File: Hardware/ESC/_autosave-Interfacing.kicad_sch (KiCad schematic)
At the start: 41 parts, among them U2 DRV8300UDRGER, U3 INA4180A2IPWR, U7 LM339

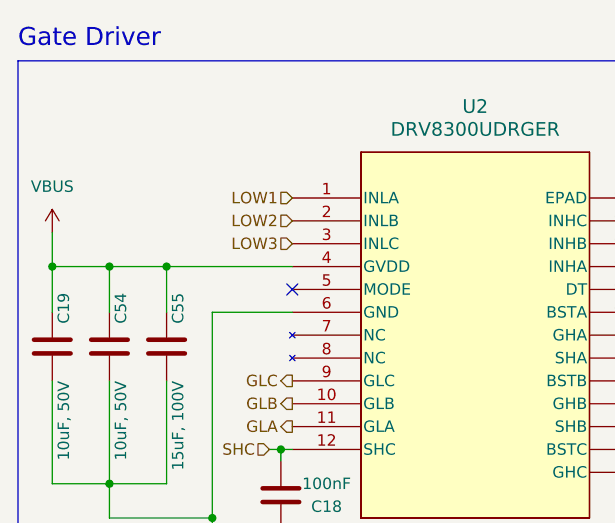
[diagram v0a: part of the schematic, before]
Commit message: Breaking + BEMF ZCD Detector
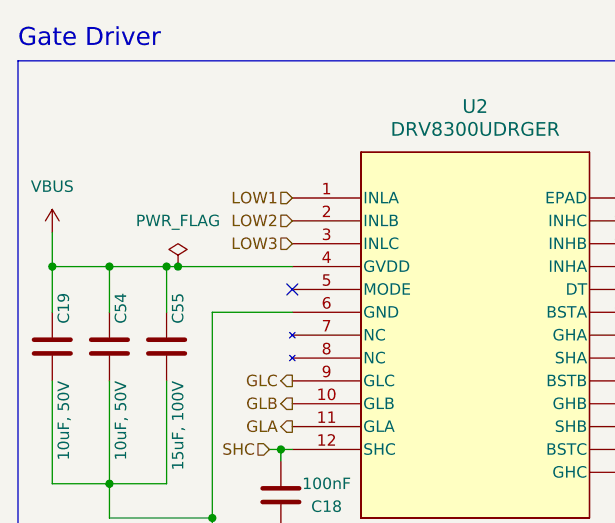
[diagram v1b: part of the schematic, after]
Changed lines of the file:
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@@
   (junction (at 132.08 139.7) (diameter 0) (color 0 0 0 0)
+  )
+  (junction (at 39.37 48.26) (diameter 0) (color 0 0 0 0)
   )
   (junction (at 31.75 72.39) (diameter 0) (color 0 0 0 0)
@@
     (stroke (width 0) (type default))
   )
-  (wire (pts (xy 38.1 48.26) (xy 52.07 48.26))
+  (wire (pts (xy 38.1 48.26) (xy 39.37 48.26))
     (stroke (width 0) (type default))
   )
@@
   )
   (wire (pts (xy 251.46 38.1) (xy 251.46 43.18))
+    (stroke (width 0) (type default))
+  )
+  (wire (pts (xy 39.37 48.26) (xy 52.07 48.26))
     (stroke (width 0) (type default))
   )
@@
     )
   )
+  (symbol (lib_id "power:PWR_FLAG") (at 39.37 48.26 0) (unit 1)
+    (in_bom yes) (on_board yes) (dnp no) (fields_autoplaced)
+    (property "Reference" "#FLG03" (at 39.37 46.355 0)
+      (effects (font (size 1.27 1.27)) hide)
+    )
+    (property "Value" "PWR_FLAG" (at 39.37 43.18 0)
+      (effects (font (size 1.27 1.27)))
+    )
+    (property "Footprint" "" (at 39.37 48.26 0)
+      (effects (font (size 1.27 1.27)) hide)
+    )
+    (property "Datasheet" "~" (at 39.37 48.26 0)
+      (effects (font (size 1.27 1.27)) hide)
+    )
+    (pin "1")
+    (instances
+      (project "BLDC_ESC"
+        (path "/bd67e774-828f-47d6-928d-7f9ad42d6cab/833552ae-4955-4bf3-a78a-8c8ee4e0e417"
+          (reference "#FLG03") (unit 1)
+        )
+      )
+    )
+  )
   (symbol (lib_id "Device:C") (at 199.39 49.53 0) (unit 1)
     (in_bom yes) (on_board yes) (dnp no) (fields_autoplaced)
@@
     )
   )
+  (symbol (lib_id "Driver_Motor:DRV8300UDRGER") (at 52.07 40.64 0) (unit 1)
+    (in_bom yes) (on_board yes) (dnp no) (fields_autoplaced)
+    (property "Reference" "U2" (at 72.39 30.48 0)
+      (effects (font (size 1.524 1.524)))
+    )
+    (property "Value" "DRV8300UDRGER" (at 72.39 33.02 0)
+      (effects (font (size 1.524 1.524)))
+    )
+    (property "Footprint" "WQFN_0DRGER_TEX" (at 52.07 40.64 0)
+      (effects (font (size 1.27 1.27) italic) hide)
+    )
+    (property "Datasheet" "DRV8300UDRGER" (at 52.07 40.64 0)
+      (effects (font (size 1.27 1.27) italic) hide)
+    )
+    (pin "1")
+    (pin "10")
+    (pin "11")
+    (pin "12")
+    (pin "13")
+    (pin "14")
+    (pin "15")
+    (pin "16")
+    (pin "17")
+    (pin "18")
+    (pin "19")
+    (pin "2")
+    (pin "20")
+    (pin "21")
+    (pin "22")
+    (pin "23")
+    (pin "24")
+    (pin "3")
+    (pin "4")
+    (pin "5")
+    (pin "7")
+    (pin "8")
+    (pin "9")
+    (pin "25")
+    (pin "6")
+    (instances
+      (project "BLDC_ESC"
+        (path "/bd67e774-828f-47d6-928d-7f9ad42d6cab/833552ae-4955-4bf3-a78a-8c8ee4e0e417"
+          (reference "U2") (unit 1)
+        )
+      )
+    )
+  )
   (symbol (lib_id "Comparator:LM339") (at 44.45 118.11 180) (unit 1)
     (in_bom yes) (on_board yes) (dnp no)
@@
         )
       )
-    )
-  )
-  (symbol (lib_id "Driver_Motor:DRV8300UDRGER") (at 52.07 40.64 0) (unit 1)
-    (in_bom yes) (on_board yes) (dnp no) (fields_autoplaced)
-    (property "Reference" "U2" (at 72.39 30.48 0)
-      (effects (font (size 1.524 1.524)))
-    )
-    (property "Value" "DRV8300UDRGER" (at 72.39 33.02 0)
-      (effects (font (size 1.524 1.524)))
-    )
-    (property "Footprint" "WQFN_0DRGER_TEX" (at 52.07 40.64 0)
-      (effects (font (size 1.27 1.27) italic) hide)
-    )
-    (property "Datasheet" "DRV8300UDRGER" (at 52.07 40.64 0)
-      (effects (font (size 1.27 1.27) italic) hide)
-    )
-    (pin "1")
-    (pin "10")
-    (pin "11")
-    (pin "12")
-    (pin "13")
-    (pin "14")
-    (pin "15")
-    (pin "16")
-    (pin "17")
-    (pin "18")
-    (pin "19")
-    (pin "2")
-    (pin "20")
-    (pin "21")
-    (pin "22")
-    (pin "23")
-    (pin "24")
-    (pin "25")
-    (pin "3")
-    (pin "4")
-    (pin "5")
-    (pin "6")
-    (pin "7")
-    (pin "8")
-    (pin "9")
-    (instances
-      (project "BLDC_ESC"
-        (path "/bd67e774-828f-47d6-928d-7f9ad42d6cab"
-          (reference "U2") (unit 1)
-        )
-        (path "/bd67e774-828f-47d6-928d-7f9ad42d6cab/833552ae-4955-4bf3-a78a-8c8ee4e0e417"
-          (reference "U2") (unit 1)
-        )
-      )
